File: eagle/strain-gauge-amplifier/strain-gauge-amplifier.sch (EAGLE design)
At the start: 25 parts, among them IC2 INA125U, M1 #4-BARE_MOUNTING_HOLE/.300, M2 #4-BARE_MOUNTING_HOLE/.300, M3 #4-BARE_MOUNTING_HOLE/.300, M4 #4-BARE_MOUNTING_HOLE/.300, Q1 PMV45EN

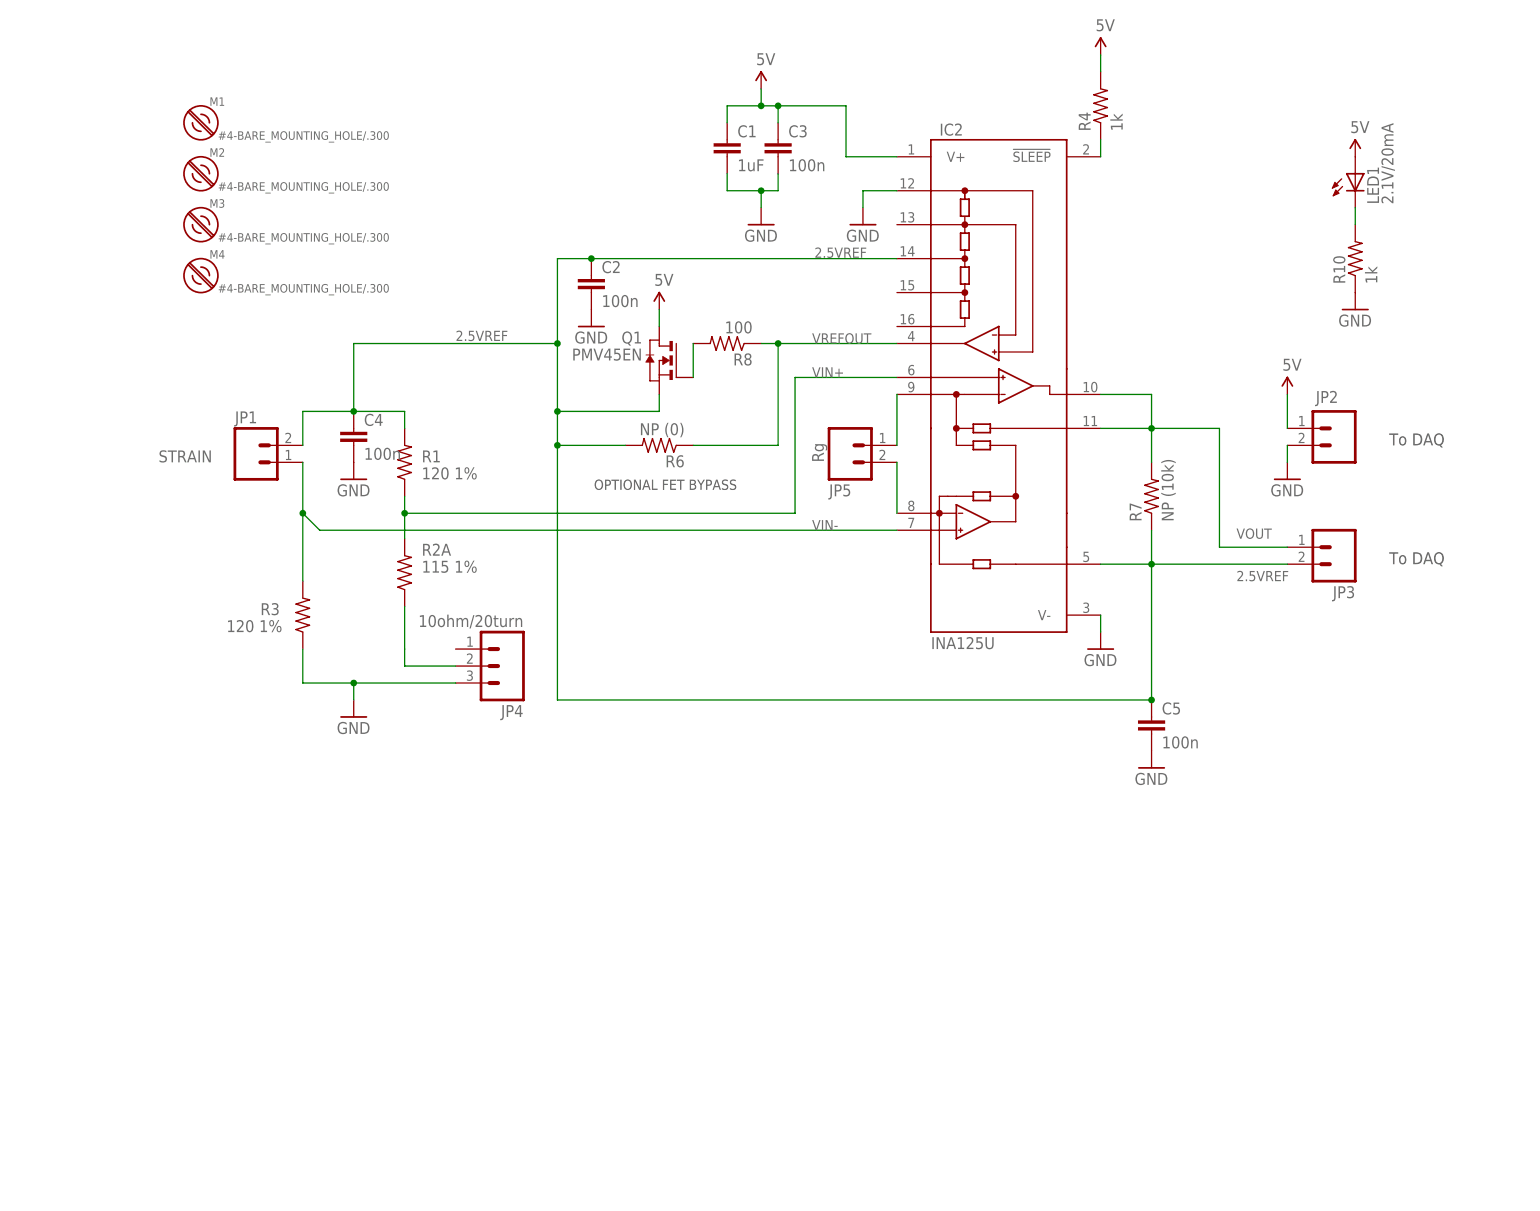
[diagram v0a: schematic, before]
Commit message: new straingauge board for 4 white strain gauge.
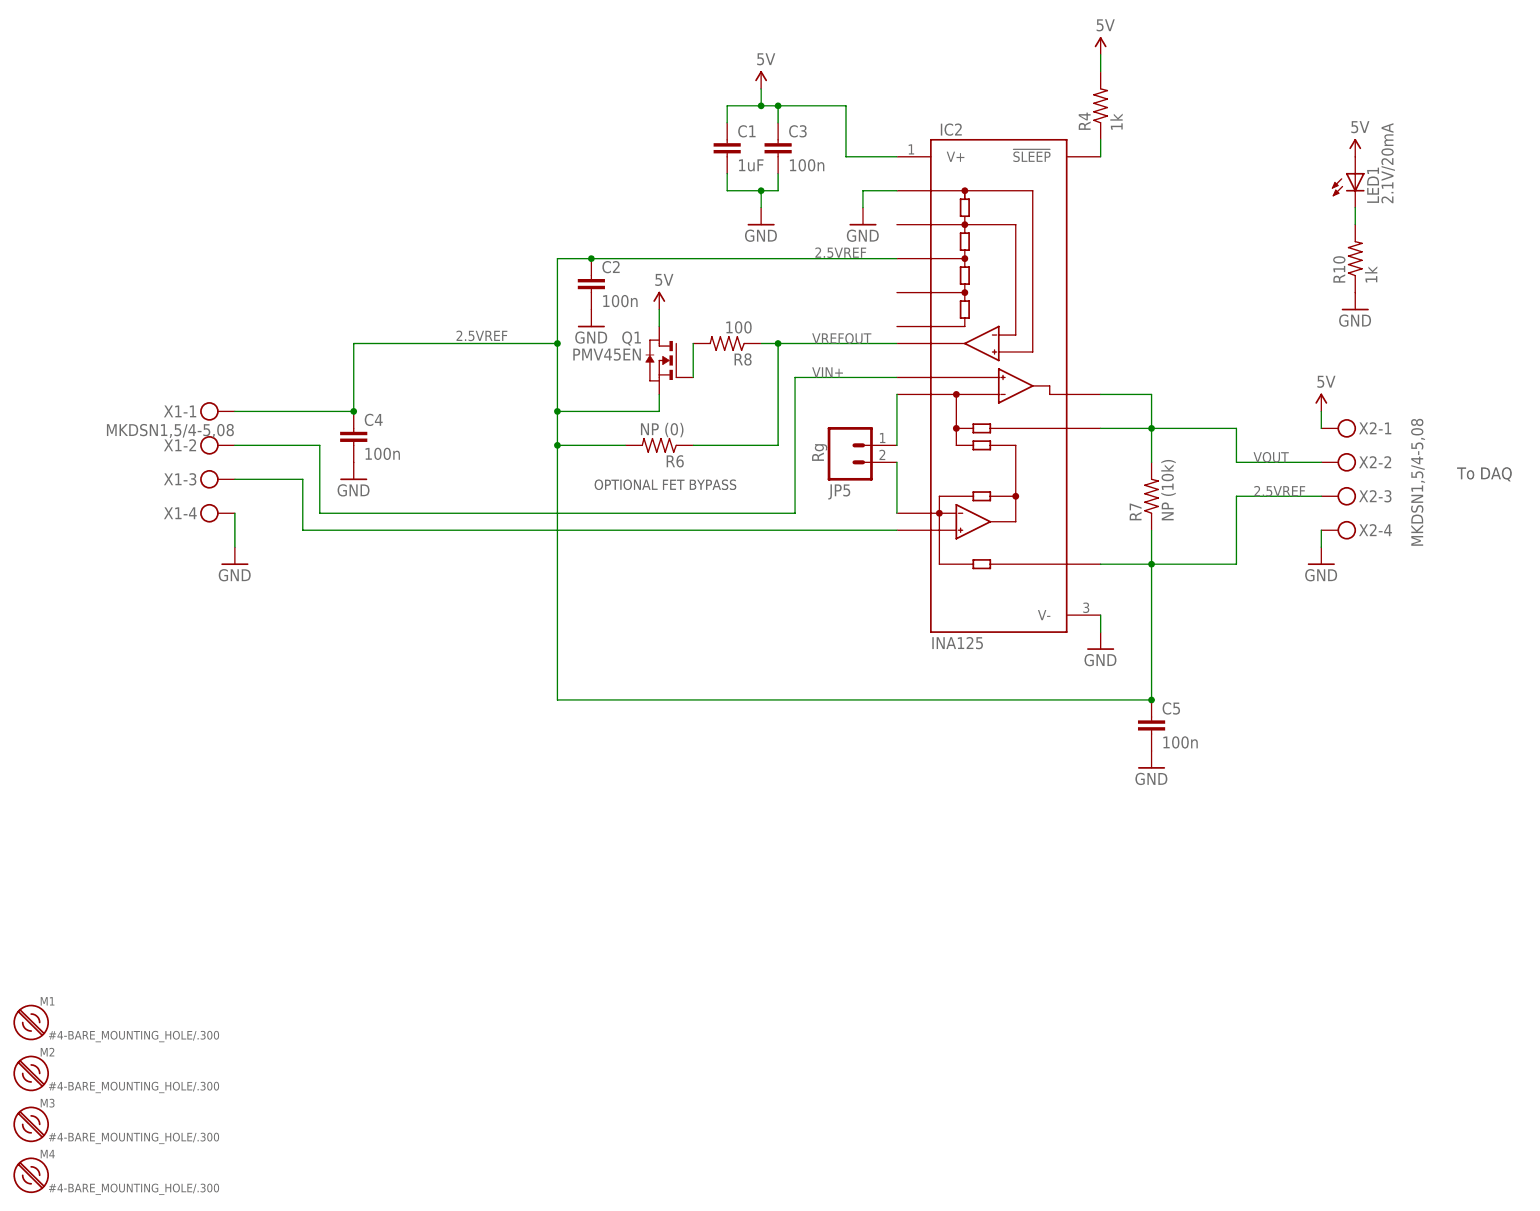
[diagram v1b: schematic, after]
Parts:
- removed JP1: STRAIN, SparkFun-Connectors:M025MM
- removed JP2, JP3: (no value), SparkFun-Connectors:M025MM
- removed JP4: 10ohm/20turn, SparkFun-Connectors:M031X03_NO_SILK
- removed R1, R3: 120 1%, rcl_custom:R-US_0805-C-NOSILK
- removed R2A: 115 1%, rcl_custom:R-US_0805-C-NOSILK
- added X1, X2: MKDSN1,5/4-5,08, con-phoenix-508:MKDSN1,5/4-5,08
- IC2: value INA125U -> INA125; device burr-brown:INA125U -> burr-brown:INA125
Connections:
- removed net N$1: JP4.2, R2A.1
- removed net VIN-: IC2.-VIN, JP1.1, R3.2
- new net N$2: IC2.-VIN, X1-3.KL
- net 2.5VREF: now also X1-1.KL, X2-3.KL; no longer JP1.2, JP3.2, R1.2
- net 5V: now also X2-1.KL; no longer JP2.1
- net GND: now also X1-4.KL, X2-4.KL; no longer JP2.2, JP4.3, R3.1
- net VIN+: now also X1-2.KL; no longer R1.1, R2A.2
- net VOUT: now also X2-2.KL; no longer JP3.1
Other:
- moved on the sheet: M1, M2, M3, M4
